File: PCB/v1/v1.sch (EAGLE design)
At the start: 56 parts, among them U2 AT24C512C-SHD-B

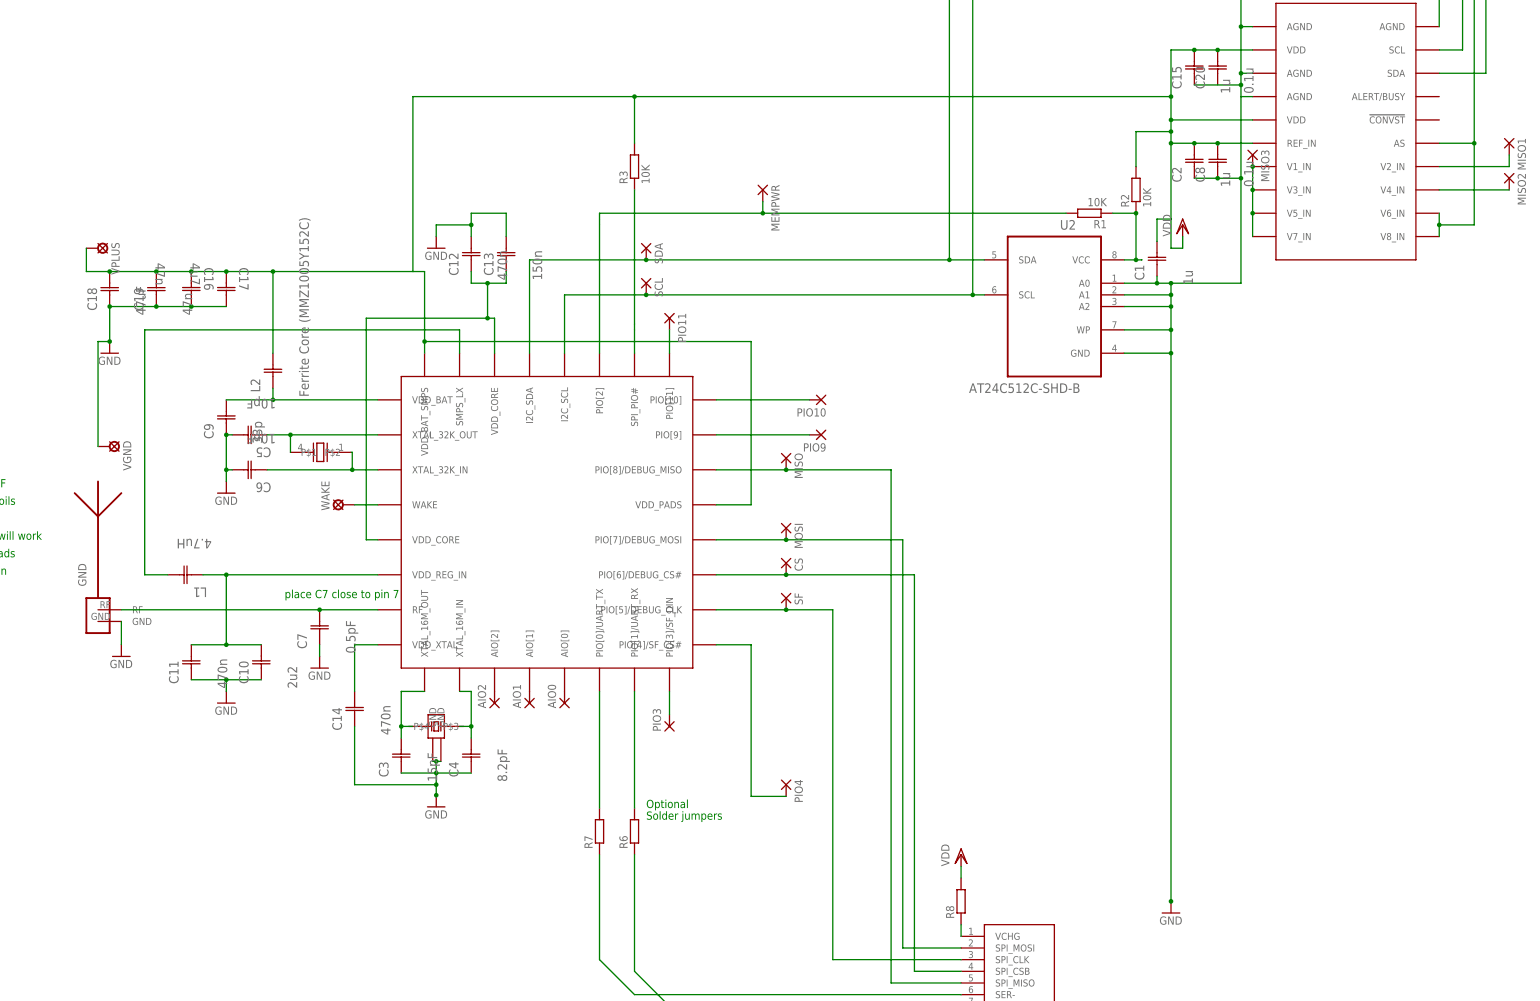
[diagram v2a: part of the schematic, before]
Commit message: watanya design. needs tweaking. RF. Want to pull components in tighter
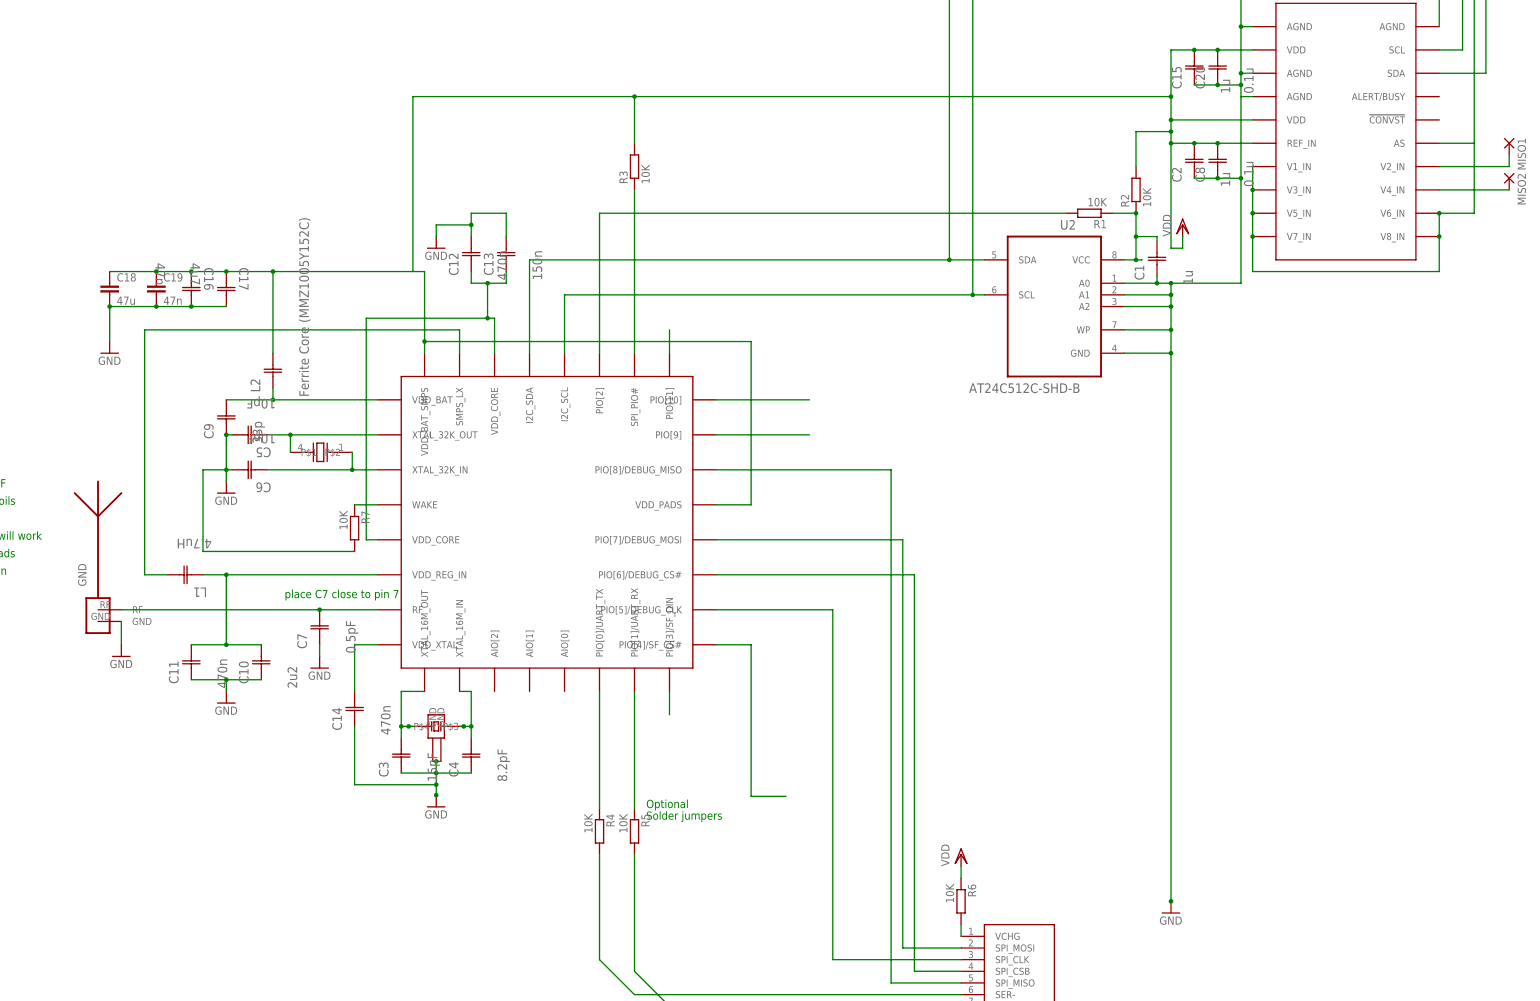
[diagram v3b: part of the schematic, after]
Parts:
- removed AIO0, AIO1, AIO2, CS, MEMPWR, MISO, MISO3, MOSI, PIO10, PIO11, PIO3, PIO4, PIO9, SCL, SDA, SF: (no value), wirepad:1,6/0,8
- removed R8: (no value), eagle-ltspice:RR1206
- removed VGND: LSP10, solpad:LSP10
- removed VPLUS, WAKE: Vrail, solpad:LSP10
- added R4, R5: 10K, rcl:R-EU_R0402
- C18: value 47uF -> 47u; device AVX_By_element14_Batch_1:0805AA100MAT1A -> resistor:C-EUC0805
- C19: device AVX_By_element14_Batch_1:0805AA100MAT1A -> rcl:C-EUC0402
- R6, R7: value (none) -> 10K; device eagle-ltspice:RR1206 -> rcl:R-EU_R0402
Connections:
- removed net N$17: AIO2.P, U$1.AIO[2]
- removed net N$33: AIO1.P, U$1.AIO[1]
- removed net N$41: AIO0.P, U$1.AIO[0]
- removed net N$88: MISO3.P, U$5.V1_IN, U$5.V3_IN, U$5.V5_IN, U$5.V7_IN
- removed net N$90: U$5.V6_IN, U$5.V8_IN
- net GND: now also C18.2, C19.2, C20.C1, R7.2, U$5.V1_IN, U$5.V3_IN, U$5.V5_IN, U$5.V6_IN, U$5.V7_IN, U$5.V8_IN; no longer C18.C1, C19.C1, VGND.MP
- net N$1: no longer PIO11.P
- net N$18: no longer MISO.P
- net N$2: no longer PIO9.P
- net N$20: now also R4.2; no longer R7.1
- net N$23: no longer PIO3.P
- net N$25: no longer PIO4.P
- net N$29: now also U$3.P$3
- net N$3: no longer MEMPWR.P
- net N$30: now also U$3.P$4
- net N$31: no longer CS.P
- net N$36: now also R5.2; no longer R6.1
- net N$37: now also R4.1; no longer R7.2
- net N$38: now also R5.1; no longer R6.2
- net N$4: now also C1.C2
- net N$40: now also R6.2; no longer R8.1
- net N$49: now also R7.1; no longer WAKE.MP
- net N$5: no longer PIO10.P
- net N$50: no longer MOSI.P
- net N$51: no longer SF.P
- net SCL: no longer SCL.P
- net SDA: no longer SDA.P
- net VDD: now also C18.1, C19.1, R6.1; no longer C1.C2, C18.C2, C19.C2, R8.2, VPLUS.MP
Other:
- moved on the sheet: R6, R7

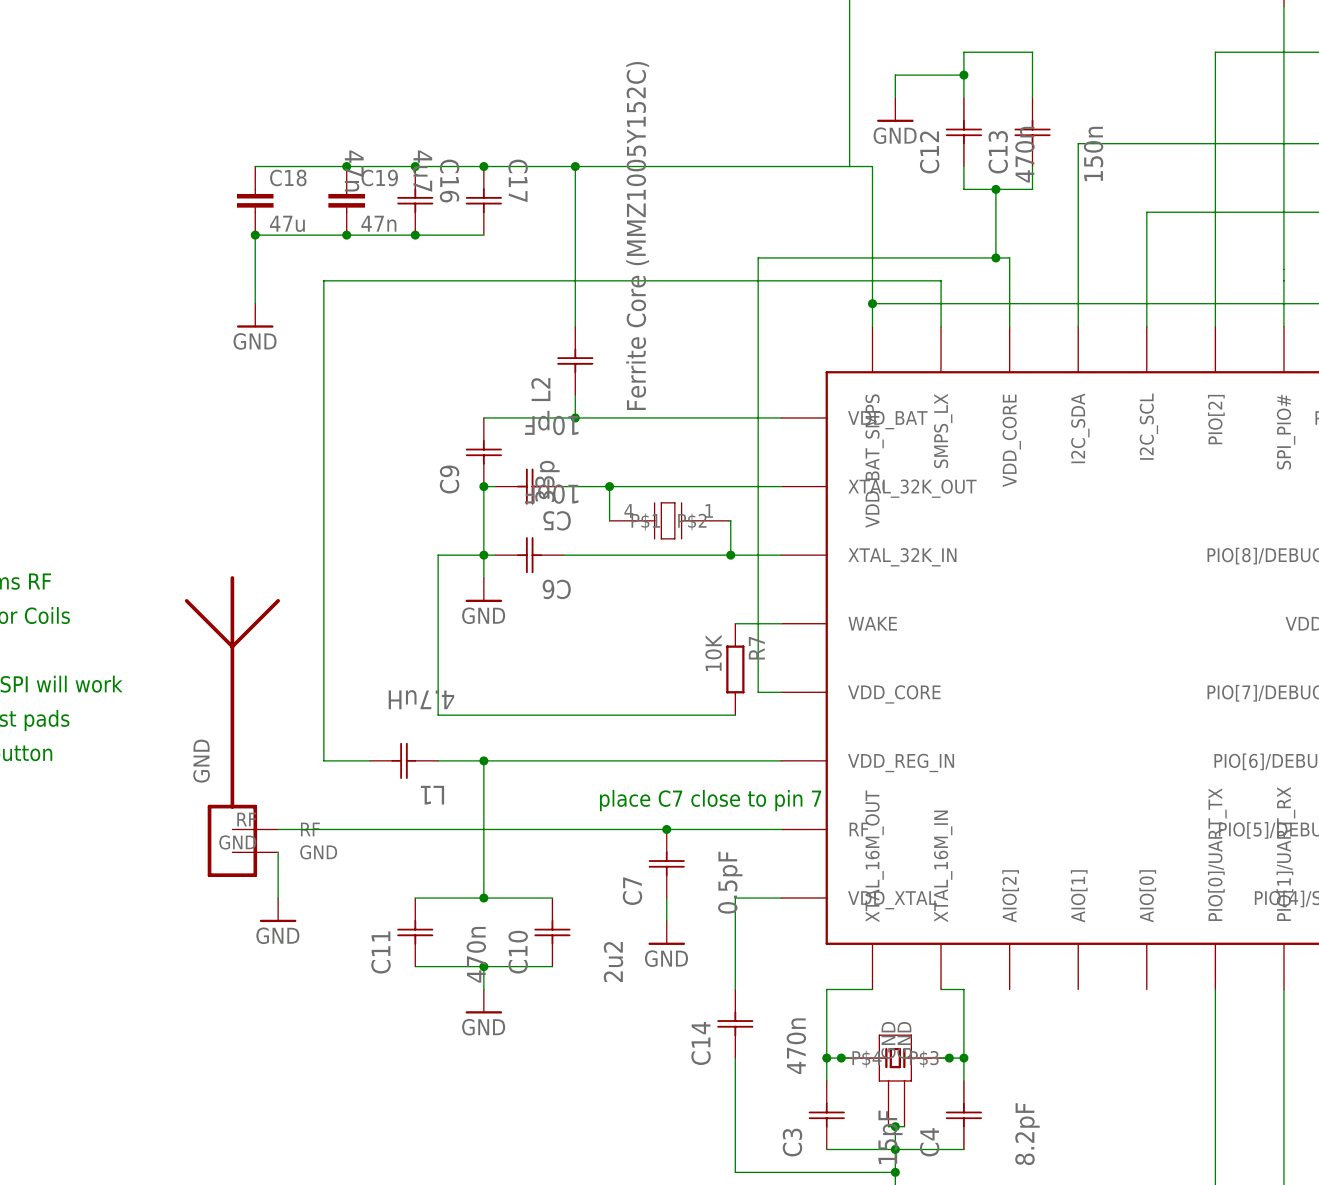
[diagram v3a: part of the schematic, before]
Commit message: making more like manufacturing kit
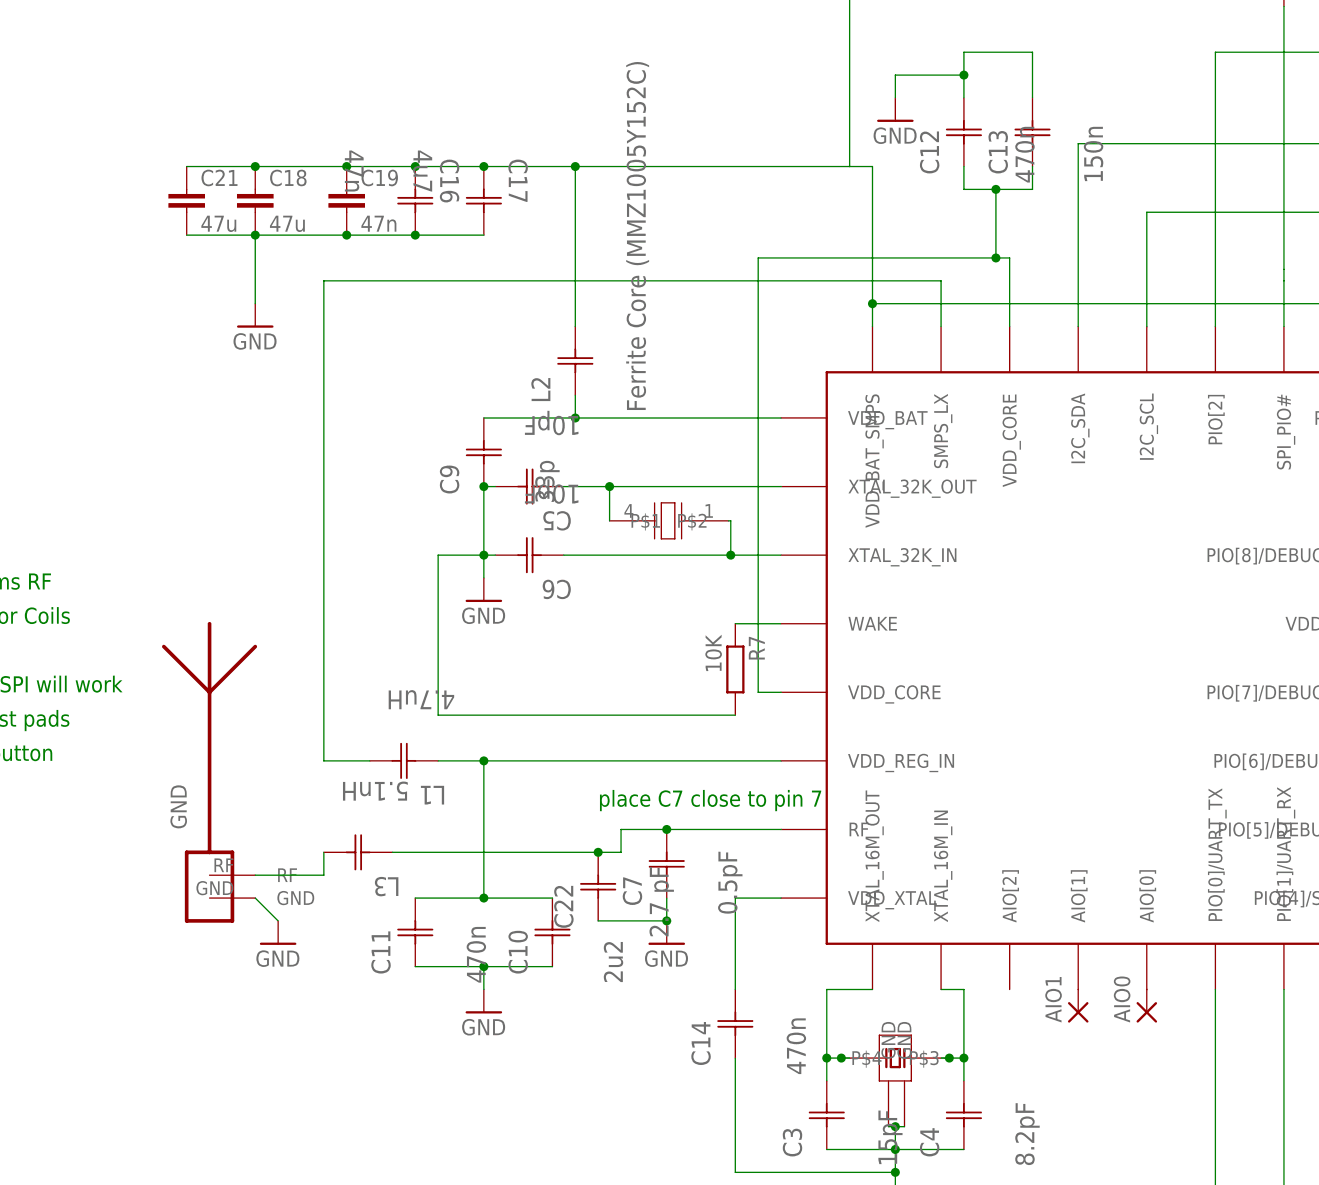
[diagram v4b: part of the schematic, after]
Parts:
- added AIO0, AIO1: (no value), wirepad:1,6/0,8
- added C21: 47u, resistor:C-EUC0805
- added C22: 2.7 pF, AVX_By_element14_Batch_1:UQCL2A0R5BAT2A/500
- added L3: 5.1nH, AVX_By_element14_Batch_1:12107C102JAT2A
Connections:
- new net N$28: AIO0.P, U$1.AIO[0]
- new net N$33: AIO1.P, U$1.AIO[1]
- new net N$34: L3.C2
- net GND: now also C21.2, C22.C1
- net N$43: now also C22.C2, L3.C1
- net VDD: now also C21.1
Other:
- moved on the sheet: GND
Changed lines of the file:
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@@
 <part name="R6" library="rcl" deviceset="R-EU_" device="R0402" value="10K"/>
 <part name="R7" library="rcl" deviceset="R-EU_" device="R0402" value="10K"/>
+<part name="AIO0" library="wirepad" deviceset="1,6/0,8" device=""/>
+<part name="AIO1" library="wirepad" deviceset="1,6/0,8" device=""/>
+<part name="C21" library="resistor" deviceset="C-EU" device="C0805" value="47u"/>
+<part name="L3" library="AVX_By_element14_Batch_1" deviceset="12107C102JAT2A" device="" value="5.1nH"/>
+<part name="C22" library="AVX_By_element14_Batch_1" deviceset="UQCL2A0R5BAT2A/500" device="" value="2.7 pF"/>
 </parts>
 <sheets>
@@
 <instance part="GND7" gate="1" x="-129.54" y="15.24"/>
 <instance part="C14" gate="A" x="-101.6" y="10.16" rot="R90"/>
-<instance part="GND9" gate="1" x="-152.4" y="25.4"/>
+<instance part="GND9" gate="1" x="-152.4" y="22.86"/>
 <instance part="C16" gate="A" x="-137.16" y="109.22" rot="R270"/>
 <instance part="C17" gate="A" x="-129.54" y="109.22" rot="R270"/>
@@
 <instance part="U$2" gate="G$1" x="43.18" y="-48.26"/>
 <instance part="U$4" gate="G$1" x="-109.22" y="69.85" rot="R270"/>
-<instance part="GND" gate="G$1" x="-157.48" y="45.72"/>
+<instance part="GND" gate="G$1" x="-160.02" y="40.64"/>
 <instance part="U$1" gate="G$1" x="-58.42" y="55.88"/>
 <instance part="C2" gate="A" x="81.28" y="129.54" rot="R90"/>
@@
 <instance part="R6" gate="G$1" x="30.48" y="-27.94" rot="R270"/>
 <instance part="R7" gate="G$1" x="-101.6" y="53.34" rot="R270"/>
+<instance part="AIO0" gate="P" x="-55.88" y="15.24" rot="R90"/>
+<instance part="AIO1" gate="P" x="-63.5" y="15.24" rot="R90"/>
+<instance part="C21" gate="G$1" x="-162.56" y="106.68"/>
+<instance part="L3" gate="A" x="-139.7" y="33.02" rot="R180"/>
+<instance part="C22" gate="A" x="-116.84" y="25.4" rot="R90"/>
 </instances>
 <busses>
@@
 <pinref part="GND5" gate="1" pin="GND"/>
 <wire x1="-109.22" y1="27.94" x2="-109.22" y2="25.4" width="0.1524" layer="91"/>
+<pinref part="C22" gate="A" pin="C1"/>
+<wire x1="-116.84" y1="25.4" x2="-109.22" y2="25.4" width="0.1524" layer="91"/>
+<junction x="-109.22" y="25.4"/>
 </segment>
 <segment>
@@
 <segment>
 <pinref part="GND9" gate="1" pin="GND"/>
-<wire x1="-152.4" y1="33.02" x2="-152.4" y2="27.94" width="0.1524" layer="91"/>
+<wire x1="-154.94" y1="27.94" x2="-152.4" y2="25.4" width="0.1524" layer="91"/>
 </segment>
 <segment>
@@
 <wire x1="-144.78" y1="101.6" x2="-137.16" y2="101.6" width="0.1524" layer="91"/>
 <junction x="-144.78" y="101.6"/>
+<pinref part="C21" gate="G$1" pin="2"/>
+<wire x1="-162.56" y1="101.6" x2="-154.94" y2="101.6" width="0.1524" layer="91"/>
 </segment>
 <segment>
@@
 <junction x="-119.38" y="109.22"/>
 <junction x="-129.54" y="109.22"/>
+<pinref part="C21" gate="G$1" pin="1"/>
+<wire x1="-154.94" y1="109.22" x2="-162.56" y2="109.22" width="0.1524" layer="91"/>
+<junction x="-154.94" y="109.22"/>
 </segment>
 <segment>
@@
 <pinref part="C7" gate="A" pin="C2"/>
 <wire x1="-96.52" y1="35.56" x2="-109.22" y2="35.56" width="0.1524" layer="91"/>
-<wire x1="-109.22" y1="35.56" x2="-152.4" y2="35.56" width="0.1524" layer="91"/>
+<pinref part="U$1" gate="G$1" pin="RF"/>
+<pinref part="L3" gate="A" pin="C1"/>
+<wire x1="-139.7" y1="33.02" x2="-116.84" y2="33.02" width="0.1524" layer="91"/>
+<wire x1="-116.84" y1="33.02" x2="-114.3" y2="33.02" width="0.1524" layer="91"/>
+<wire x1="-114.3" y1="33.02" x2="-114.3" y2="35.56" width="0.1524" layer="91"/>
+<wire x1="-114.3" y1="35.56" x2="-109.22" y2="35.56" width="0.1524" layer="91"/>
 <junction x="-109.22" y="35.56"/>
-<pinref part="U$1" gate="G$1" pin="RF"/>
+<pinref part="C22" gate="A" pin="C2"/>
+<junction x="-116.84" y="33.02"/>
 </segment>
 </net>
@@
 </segment>
 </net>
+<net name="N$28" class="0">
+<segment>
+<pinref part="U$1" gate="G$1" pin="AIO[0]"/>
+<pinref part="AIO0" gate="P" pin="P"/>
+</segment>
+</net>
+<net name="N$33" class="0">
+<segment>
+<pinref part="U$1" gate="G$1" pin="AIO[1]"/>
+<pinref part="AIO1" gate="P" pin="P"/>
+</segment>
+</net>
+<net name="N$34" class="0">
+<segment>
+<pinref part="L3" gate="A" pin="C2"/>
+<wire x1="-154.94" y1="30.48" x2="-147.32" y2="30.48" width="0.1524" layer="91"/>
+<wire x1="-147.32" y1="30.48" x2="-147.32" y2="33.02" width="0.1524" layer="91"/>
+</segment>
+</net>

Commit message: final check and submit
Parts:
- added MISO3, MISO4: (no value), wirepad:1,6/0,8
- C16: value 47n -> 2u2
- C17: value 4u7 -> 47n
- C19: device rcl:C-EUC0402 -> AVX_By_element14_Batch_1:UQCL2A100JAT2A/500
- L3: value 5.1nH -> Ferrite Core (MMZ1005Y152C); device AVX_By_element14_Batch_1:12107C102JAT2A -> AVX_By_element14_Batch_1:UQCL2A100JAT2A/500
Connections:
- removed net N$34: L3.C2
- new net N$73: MISO3.P, U$5.V6_IN
- new net N$83: MISO4.P, U$5.V8_IN
- new net N$87: C19.C2, U$1.VDD_PADS
- net GND: now also C19.C1; no longer C19.2, C5.C2, U$5.V3_IN, U$5.V5_IN, U$5.V6_IN, U$5.V8_IN
- net VDD: no longer C19.1, U$1.VDD_PADS
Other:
- moved on the sheet: C17, C9, MISO1, MISO2
